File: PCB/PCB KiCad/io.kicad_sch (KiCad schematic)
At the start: 6 parts

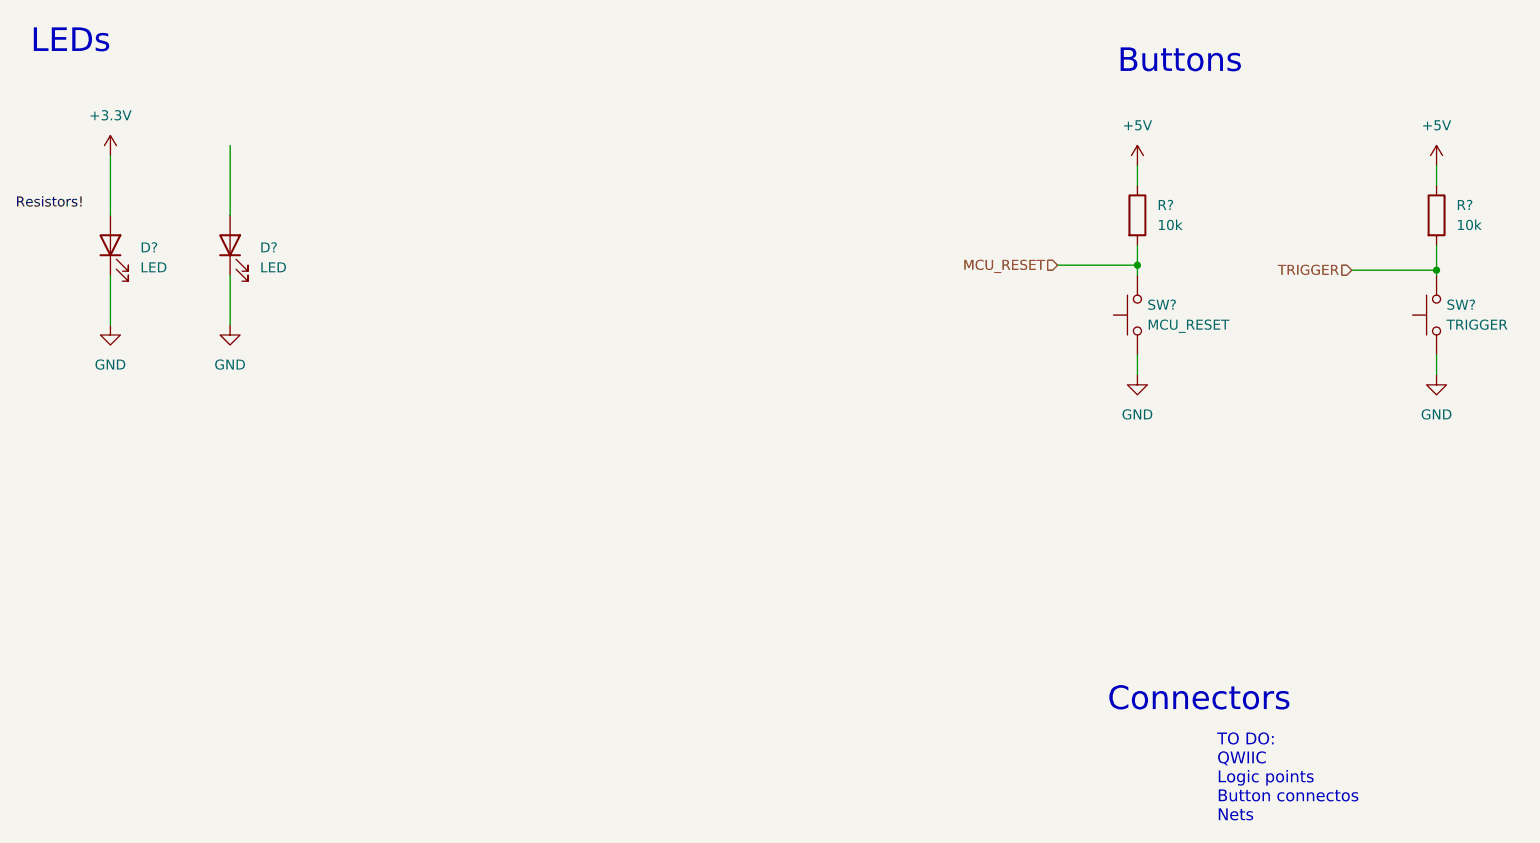
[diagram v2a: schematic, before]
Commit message: Merge MCU and IO into single sheet, wire LEDs
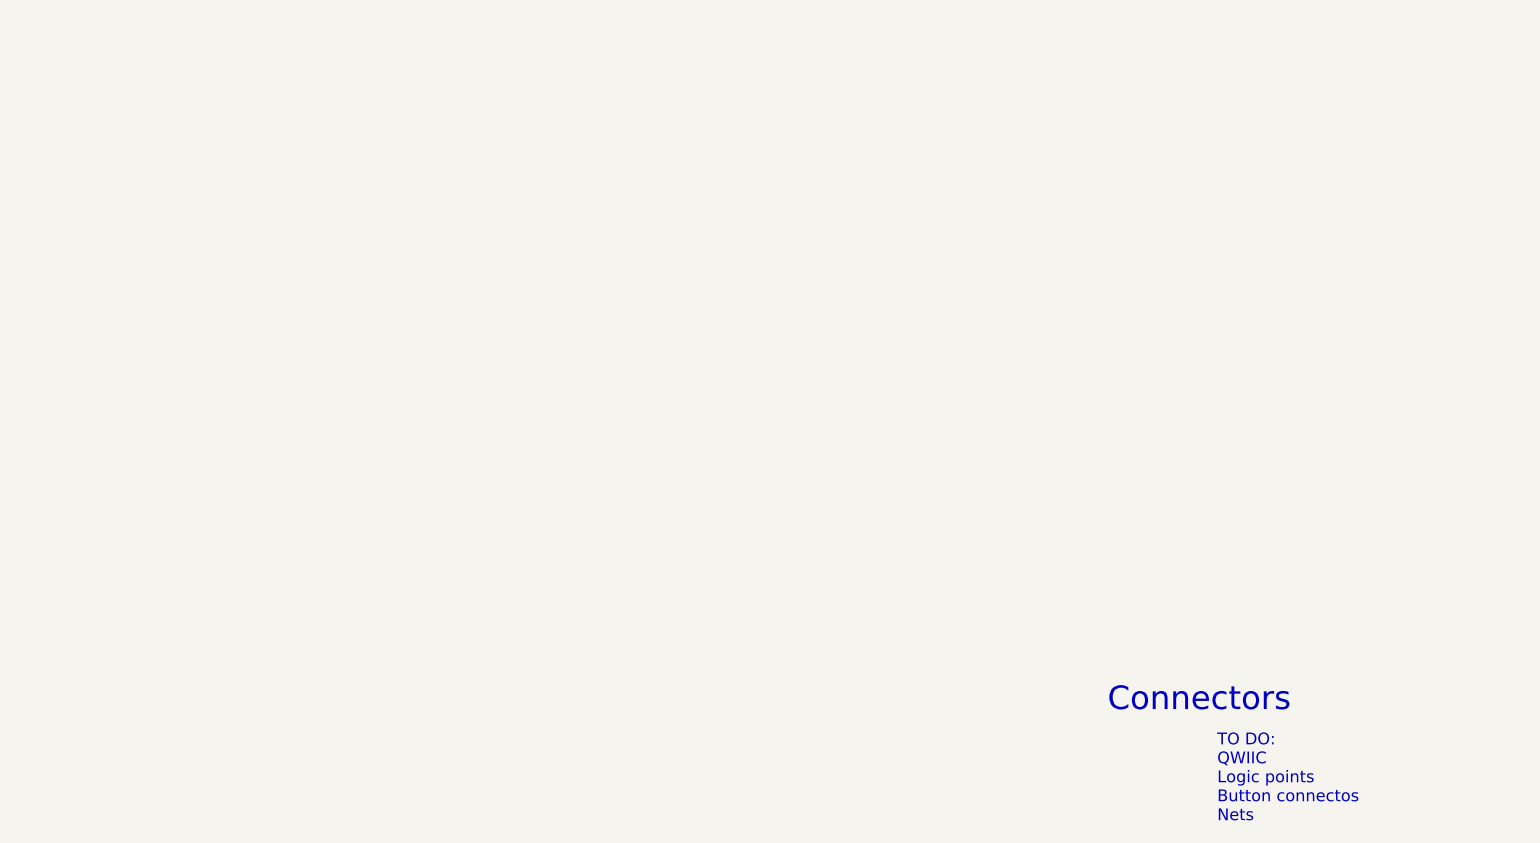
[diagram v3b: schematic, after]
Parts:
- removed D? (x2): LED, symbol Device:LED
- removed R? (x2): 10k, symbol Device:R
- removed SW?: TRIGGER, symbol Switch:SW_Push
- removed SW?: MCU_RESET, symbol Switch:SW_Push
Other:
- note removed: "Buttons"
- note removed: "LEDs"
